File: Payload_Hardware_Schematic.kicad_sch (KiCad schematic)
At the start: 4 parts, among them J1 Micro_SD_Card, U1 STM32F411 BlackPill, U3 BMP388, U4 LSM9DS1

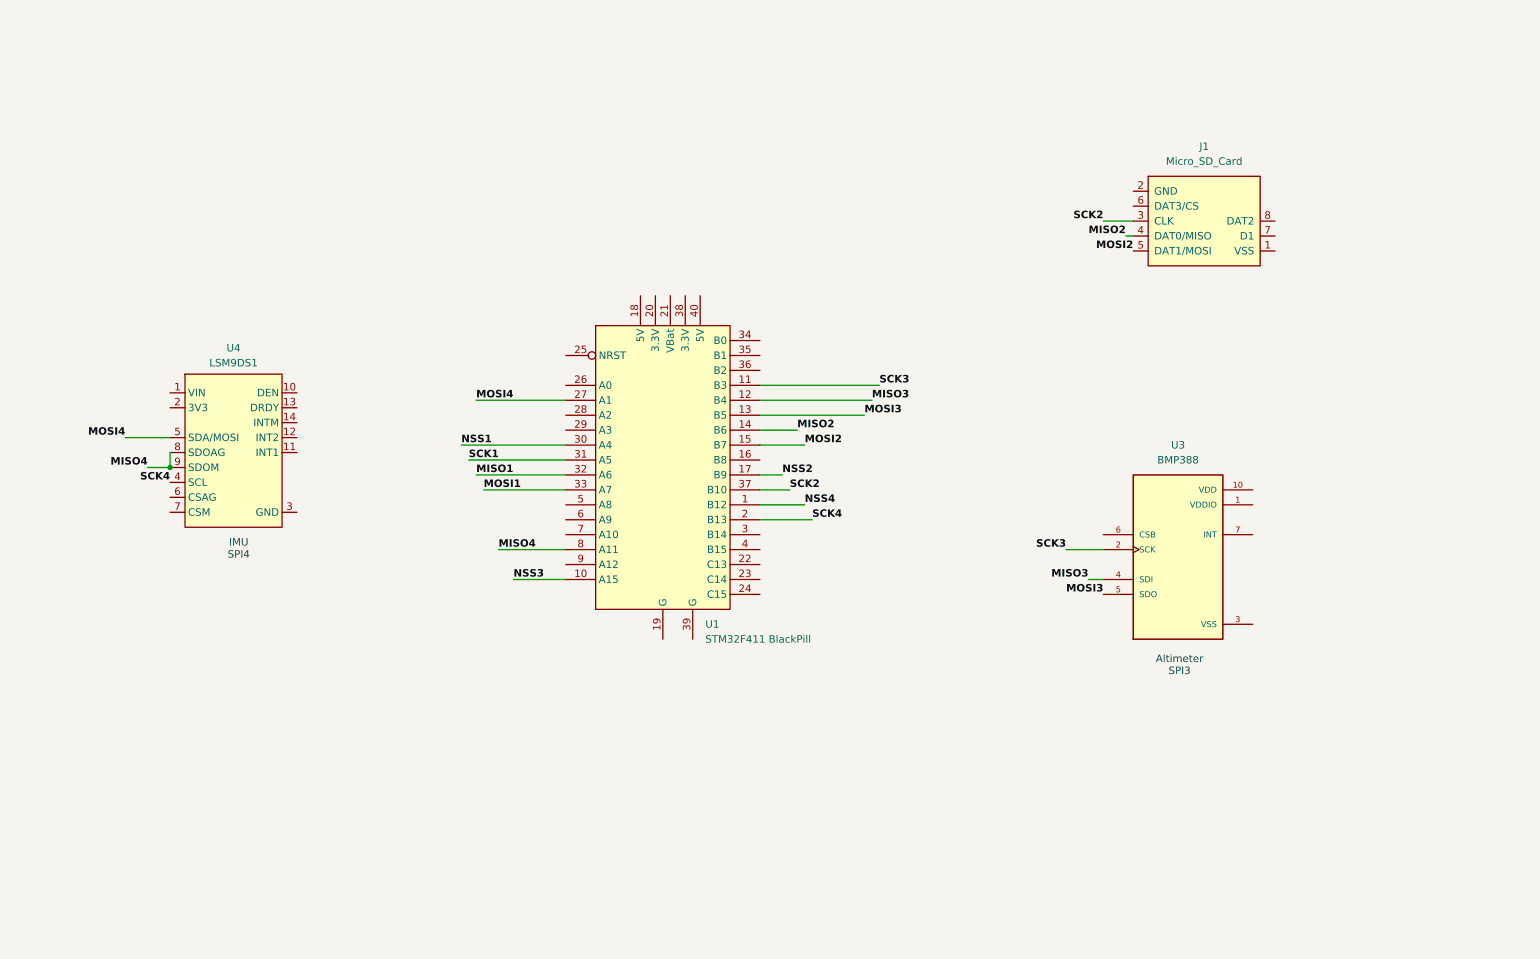
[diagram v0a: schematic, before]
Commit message: Combined Power and Electronics Schematic
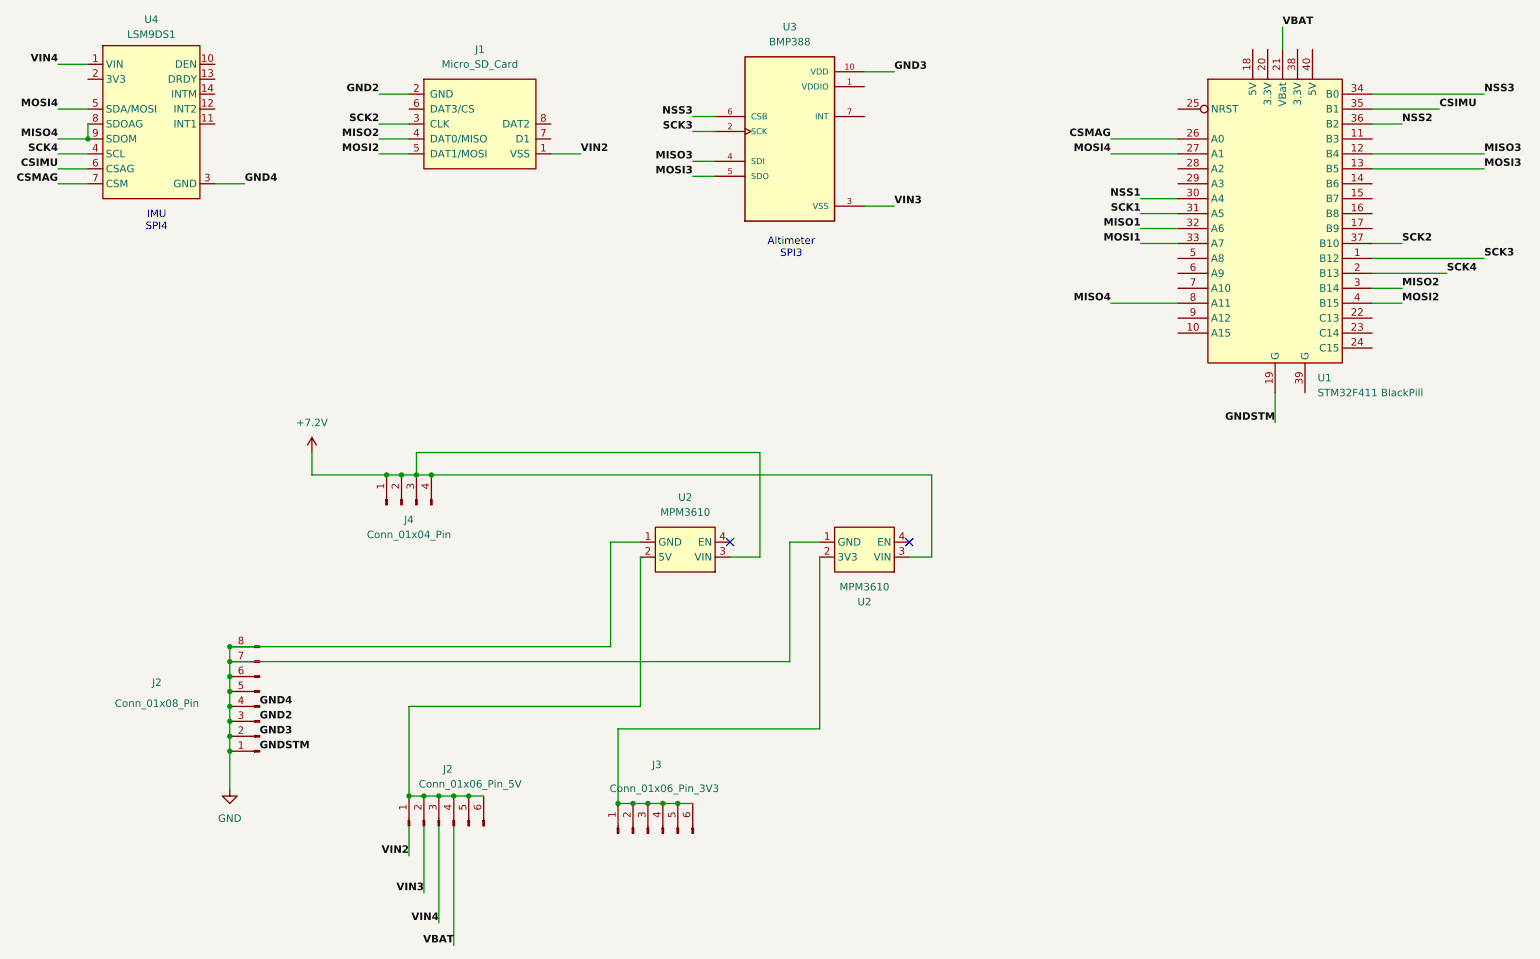
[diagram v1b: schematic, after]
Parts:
- added J2: Conn_01x06_Pin_5V, symbol Connector:Conn_01x06_Pin
- added J2: Conn_01x08_Pin, symbol Connector:Conn_01x08_Pin
- added J3: Conn_01x06_Pin_3V3, symbol Connector:Conn_01x06_Pin
- added J4: Conn_01x04_Pin, symbol Connector:Conn_01x04_Pin
- added U2 (x2): MPM3610, Footprints:MPM3610, symbol Avionics_Symbols:MPM3610
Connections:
- net NSS4 is gone; now on net SCK3: U1.1 (B12)
- net GND: now also J2.1 (Pin_1), J2.2 (Pin_2), J2.3 (Pin_3), J2.4 (Pin_4), J2.5 (Pin_5), J2.6 (Pin_6), J2.7 (Pin_7), J2.8 (Pin_8), U2.1 (GND), U2.1 (GND)
- net MISO2: now also U1.3 (B14); no longer U1.14 (B6)
- net MOSI2: now also U1.4 (B15); no longer U1.15 (B7)
- net NSS2: now also U1.36 (B2); no longer U1.17 (B9)
- net NSS3: now also U1.34 (B0), U3.6 (CSB); no longer U1.10 (A15)
- net SCK3: no longer U1.11 (B3)
- net GND3: now reaches U3.10 (VDD)
- net at J1.2 (GND): no longer names the net of J1.2 (GND)
- net VIN4: now reaches U4.1 (VIN)
- net GND4: now reaches U4.3 (GND)
- net CSIMU: now reaches U4.6 (CSAG)
- net CSIMU: now also U1.35 (B1)
- net CSMAG: now reaches U4.7 (CSM)
- net CSMAG: now also U1.26 (A0)
- net GNDSTM: now reaches U1.19 (G)
- net VBAT: now reaches U1.21 (VBat)
- new net: J3.1 (Pin_1), J3.2 (Pin_2), J3.3 (Pin_3), J3.4 (Pin_4), J3.5 (Pin_5), J3.6 (Pin_6), U2.2 (3V3)
- new net: J2.1 (Pin_1), J2.2 (Pin_2), J2.3 (Pin_3), J2.4 (Pin_4), J2.5 (Pin_5), J2.6 (Pin_6), U2.2 (5V)
- new net +7.2V: J4.1 (Pin_1), J4.2 (Pin_2), J4.3 (Pin_3), J4.4 (Pin_4), U2.3 (VIN), U2.3 (VIN)
- no-connect marks 0 -> 2
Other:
- moved on the sheet: J1, U1, U3, U4

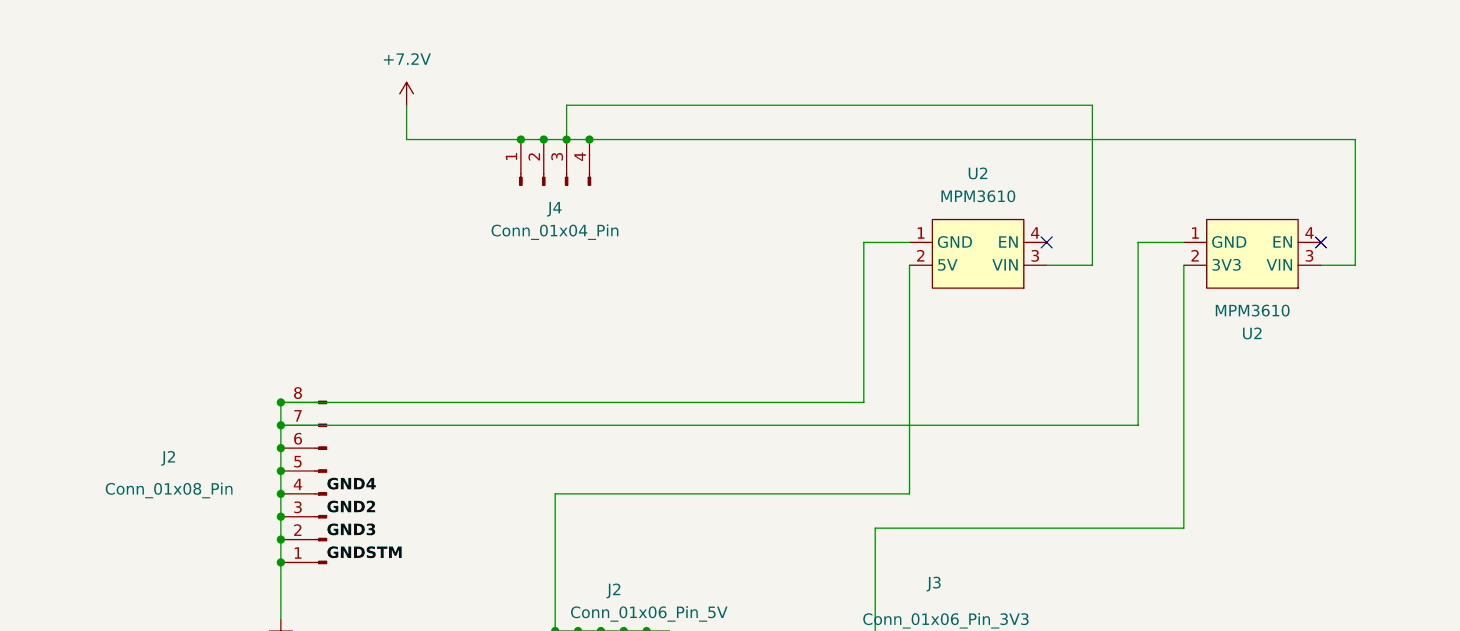
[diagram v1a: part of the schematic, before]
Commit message: Added the power regulator footprints to Footprints folder
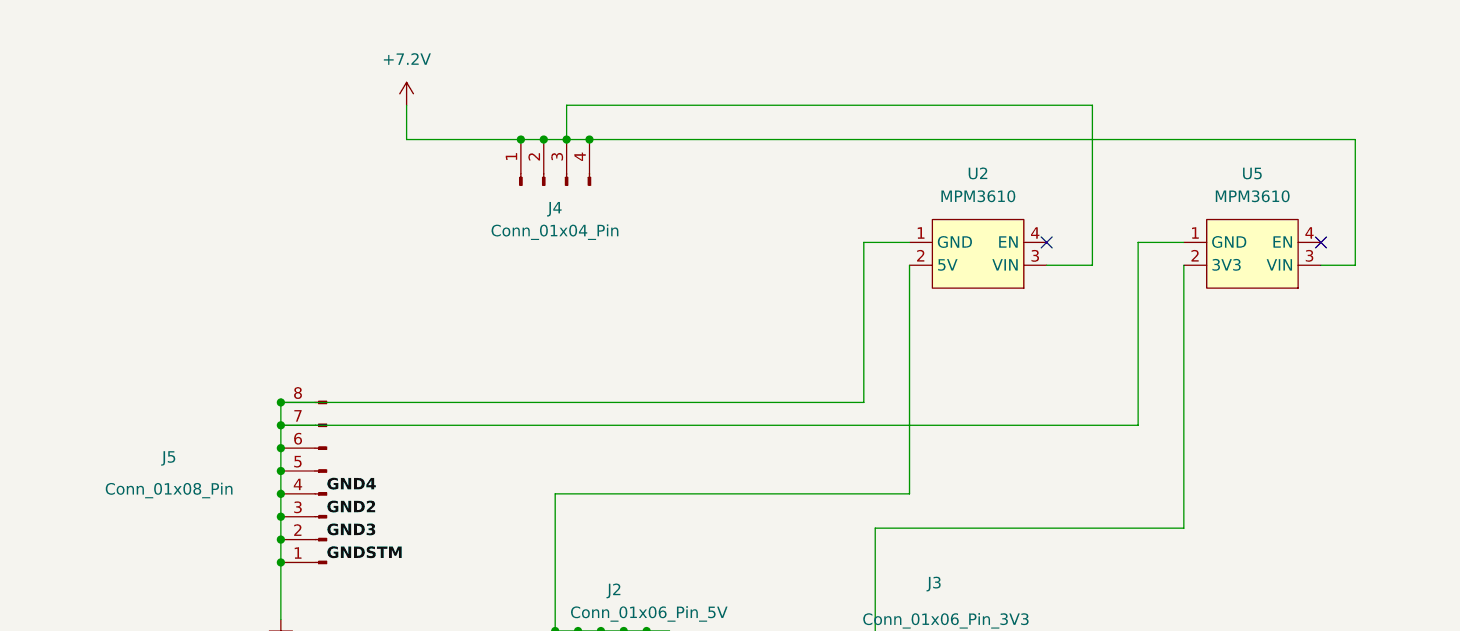
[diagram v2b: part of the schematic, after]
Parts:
- U2: footprint Footprints:MPM3610 -> PowerRegulation:MPM3610
- U5: renamed from U2; footprint Footprints:MPM3610 -> PowerRegulation:MPM3610
- renumbered J2 to J5
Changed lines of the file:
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@@
 		(dnp no)
 		(fields_autoplaced yes)
-		(property "Reference" "U2"
-			(at 166.37 118.11 0)
+		(property "Reference" "U5"
+			(at 166.37 100.33 0)
 			(effects
 				(font
@@
 		)
 		(property "Value" "MPM3610"
-			(at 166.37 115.57 0)
-			(effects
-				(font
-					(size 1.27 1.27)
-				)
-			)
-		)
-		(property "Footprint" "Footprints:MPM3610"
+			(at 166.37 102.87 0)
+			(effects
+				(font
+					(size 1.27 1.27)
+				)
+			)
+		)
+		(property "Footprint" "PowerRegulation:MPM3610"
 			(at 165.1 102.87 0)
 			(effects
@@
 			(project "Payload_Hardware_Schematic"
 				(path "/f4ead8bb-2437-4e54-a6d9-f5ca11bfd675"
-					(reference "U2")
+					(reference "U5")
 					(unit 1)
 				)
@@
 			)
 		)
-		(property "Footprint" "Footprints:MPM3610"
+		(property "Footprint" "PowerRegulation:MPM3610"
 			(at 134.62 102.87 0)
 			(effects
@@
 		(on_board yes)
 		(dnp no)
-		(property "Reference" "J2"
+		(property "Reference" "J5"
 			(at 45.212 131.826 0)
 			(effects
@@
 			(project "Payload_Hardware_Schematic"
 				(path "/f4ead8bb-2437-4e54-a6d9-f5ca11bfd675"
-					(reference "J2")
-					(unit 1)
-				)
+					(reference "J5")
+					(unit 1)
+				)

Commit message: Editted power and labels
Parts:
- added U6: ~, BMP388:BMP388_Breakout, symbol BMP388_new:BMP388_Breakout
- J2, J3: footprint (none) -> Connector_PinSocket_2.54mm:PinSocket_1x06_P2.54mm_Vertical
- J4: footprint (none) -> Connector_PinSocket_2.54mm:PinSocket_1x04_P2.54mm_Vertical
- J5: footprint (none) -> Connector_PinSocket_2.54mm:PinSocket_1x08_P2.54mm_Vertical
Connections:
- net GND3: now also U6.3 (GND)
- net MISO3: now also U6.5 (SDO)
- net MOSI3: now also U6.6 (SDA)
- net NSS3: now also U6.7 (CS)
- net SCK3: now also U6.4 (SCL)
- net VSS: now also U6.1 (VIN)
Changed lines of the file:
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@@
+	)
+	(label "VIN3"
+		(at 111.76 80.01 0)
+		(effects
+			(font
+				(size 1.27 1.27)
+				(thickness 0.254)
+				(bold yes)
+				(color 0 0 194 1)
+			)
+			(justify left bottom)
+		)
 	)
 	(label "VIN3"
@@
 		)
 	)
+	(label "SCK3"
+		(at 111.76 72.39 0)
+		(effects
+			(font
+				(size 1.27 1.27)
+				(thickness 0.254)
+				(bold yes)
+				(color 23 39 255 1)
+			)
+			(justify left bottom)
+		)
+	)
 	(label "GND2"
 		(at 63.5 138.43 0)
@@
 		)
 	)
+	(label "MISO3"
+		(at 111.76 69.85 0)
+		(effects
+			(font
+				(size 1.27 1.27)
+				(thickness 0.254)
+				(bold yes)
+				(color 23 39 255 1)
+			)
+			(justify left bottom)
+		)
+	)
 	(label "VIN3"
 		(at 91.44 167.64 180)
@@
 		)
 	)
+	(label "GND3"
+		(at 111.76 74.93 0)
+		(effects
+			(font
+				(size 1.27 1.27)
+				(thickness 0.254)
+				(bold yes)
+				(color 0 0 194 1)
+			)
+			(justify left bottom)
+		)
+	)
 	(label "VIN4"
 		(at 29.21 26.67 180)
@@
 		)
 	)
+	(label "NSS3"
+		(at 111.76 64.77 0)
+		(effects
+			(font
+				(size 1.27 1.27)
+				(thickness 0.254)
+				(bold yes)
+				(color 23 39 255 1)
+			)
+			(justify left bottom)
+		)
+	)
 	(label "MISO4"
 		(at 208.28 67.31 180)
@@
 			)
 			(justify right bottom)
+		)
+	)
+	(label "MOSI3"
+		(at 111.76 67.31 0)
+		(effects
+			(font
+				(size 1.27 1.27)
+				(thickness 0.254)
+				(bold yes)
+				(color 23 39 255 1)
+			)
+			(justify left bottom)
 		)
 	)
@@
 			)
 		)
-		(property "Footprint" ""
+		(property "Footprint" "Connector_PinSocket_2.54mm:PinSocket_1x06_P2.54mm_Vertical"
 			(at 129.54 157.48 0)
 			(effects
@@
 			)
 		)
-		(property "Footprint" ""
+		(property "Footprint" "Connector_PinSocket_2.54mm:PinSocket_1x06_P2.54mm_Vertical"
 			(at 93.98 156.21 0)
 			(effects
@@
 		(pin "7"
 		)
+		(pin "9"
+		)
 		(instances
 			(project "Payload_Hardware_Schematic"
 				(path "/f4ead8bb-2437-4e54-a6d9-f5ca11bfd675"
 					(reference "J1")
+					(unit 1)
+				)
+			)
+		)
+	)
+	(symbol
+		(lib_id "BMP388_new:BMP388_Breakout")
+		(at 105.41 68.58 90)
+		(unit 1)
+		(exclude_from_sim no)
+		(in_bom yes)
+		(on_board yes)
+		(dnp no)
+		(fields_autoplaced yes)
+		(property "Reference" "U6"
+			(at 102.5525 54.61 90)
+			(effects
+				(font
+					(size 1.27 1.27)
+				)
+			)
+		)
+		(property "Value" "~"
+			(at 102.5525 57.15 90)
+			(effects
+				(font
+					(size 1.27 1.27)
+				)
+			)
+		)
+		(property "Footprint" "BMP388:BMP388_Breakout"
+			(at 105.41 68.58 0)
+			(effects
+				(font
+					(size 1.27 1.27)
+				)
+				(hide yes)
+			)
+		)
+		(property "Datasheet" ""
+			(at 105.41 68.58 0)
+			(effects
+				(font
+					(size 1.27 1.27)
+				)
+				(hide yes)
+			)
+		)
+		(property "Description" ""
+			(at 105.41 68.58 0)
+			(effects
+				(font
+					(size 1.27 1.27)
+				)
+				(hide yes)
+			)
+		)
+		(pin "1"
+		)
+		(pin "3"
+		)
+		(pin "8"
+		)
+		(pin "2"
+		)
+		(pin "6"
+		)
+		(pin "7"
+		)
+		(pin "5"
+		)
+		(pin "4"
+		)
+		(instances
+			(project ""
+				(path "/f4ead8bb-2437-4e54-a6d9-f5ca11bfd675"
+					(reference "U6")
 					(unit 1)
 				)
@@
 			)
 		)
-		(property "Footprint" ""
+		(property "Footprint" "Connector_PinSocket_2.54mm:PinSocket_1x08_P2.54mm_Vertical"
 			(at 63.5 135.89 0)
 			(effects
@@
 			)
 		)
-		(property "Footprint" ""
+		(property "Footprint" "Connector_PinSocket_2.54mm:PinSocket_1x04_P2.54mm_Vertical"
 			(at 87.63 101.6 0)
 			(effects
